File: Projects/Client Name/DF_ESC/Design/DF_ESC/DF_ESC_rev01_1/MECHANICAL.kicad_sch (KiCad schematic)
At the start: 0 parts

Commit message: libraries & schemtics
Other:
- note added: "03407610395"
- note added: "Muhammad Moiz"
- note added: "moizrai765yt@gmail.com"
- company: (none) -> coVenture
- title: (none) -> MECHANICAL
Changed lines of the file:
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@@
 	(generator_version "8.0")
 	(paper "A4")
+	(title_block
+		(title "MECHANICAL")
+		(date "2025-02-03")
+		(rev "rev01_1")
+		(company "coVenture")
+	)
+	(text "Muhammad Moiz\n"
+		(exclude_from_sim no)
+		(at 210.566 168.656 0)
+		(effects
+			(font
+				(size 1.27 1.27)
+			)
+		)
+	)
+	(text "moizrai765yt@gmail.com\n"
+		(exclude_from_sim no)
+		(at 214.63 171.704 0)
+		(effects
+			(font
+				(size 1.27 1.27)
+			)
+		)
+	)
+	(text "03407610395\n"
+		(exclude_from_sim no)
+		(at 209.55 177.8 0)
+		(effects
+			(font
+				(size 1.27 1.27)
+			)
+		)
+	)
 )

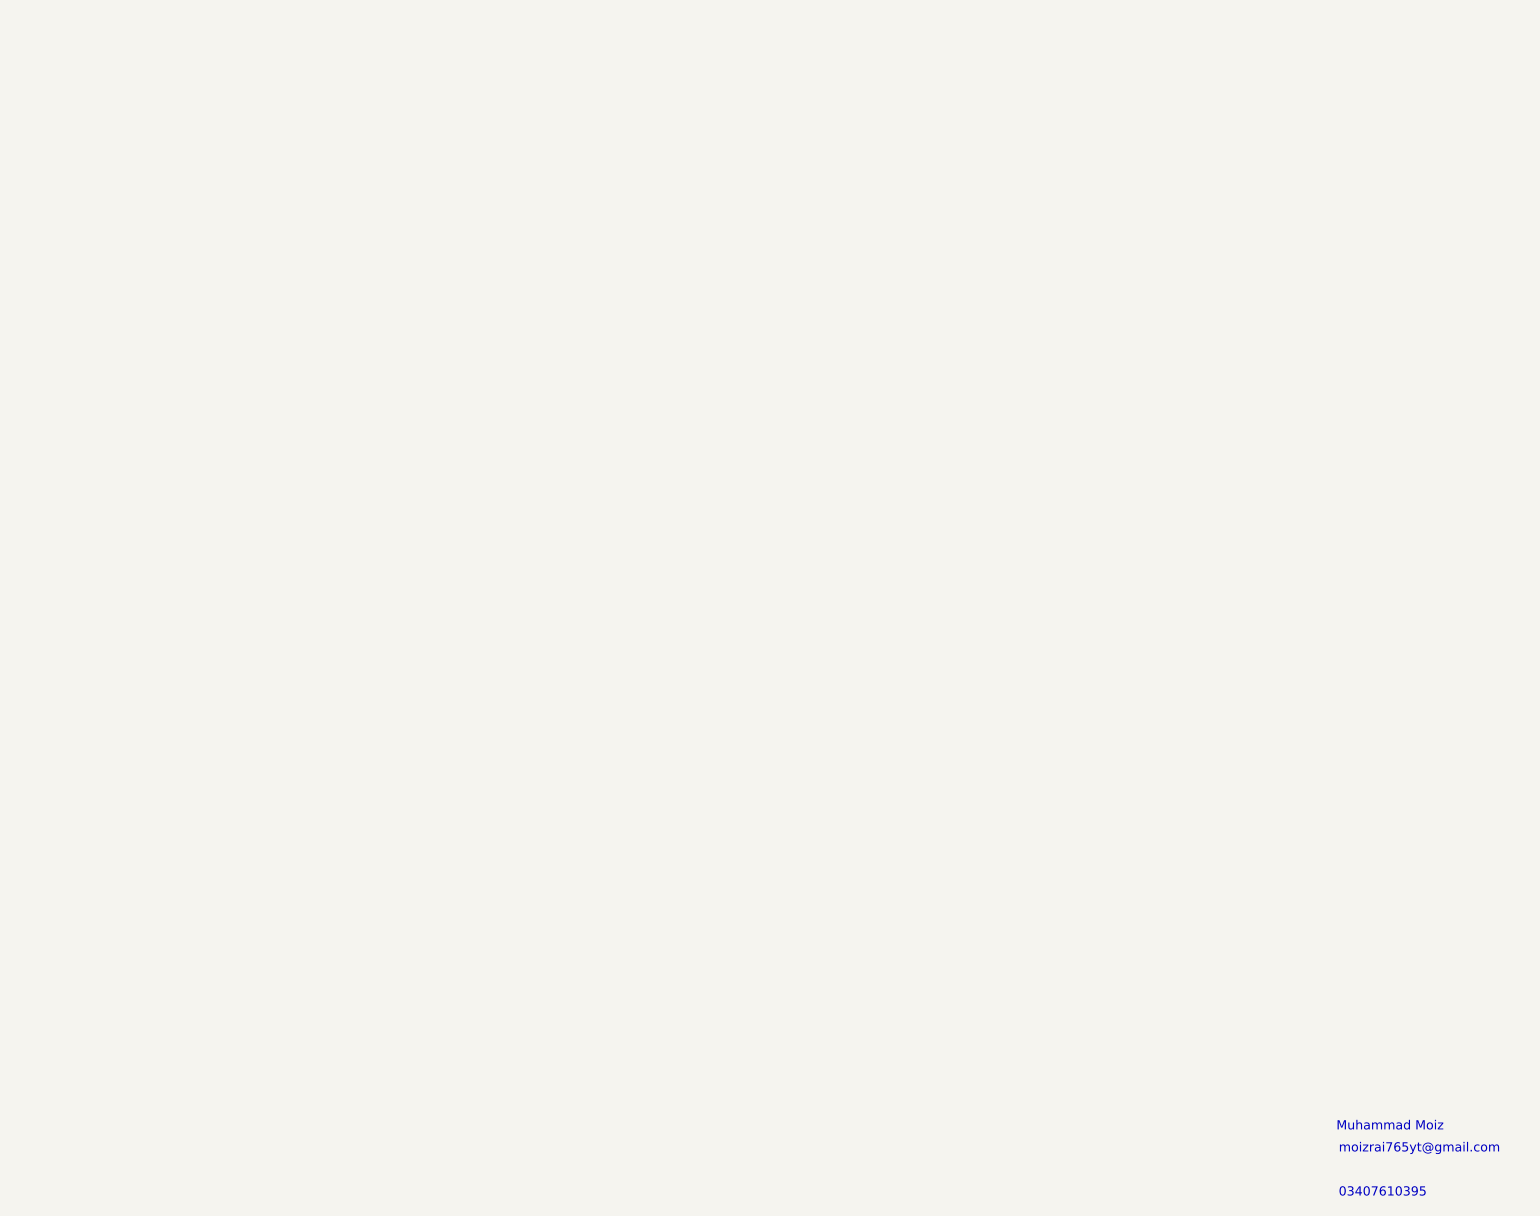
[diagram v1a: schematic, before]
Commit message: updated footprints
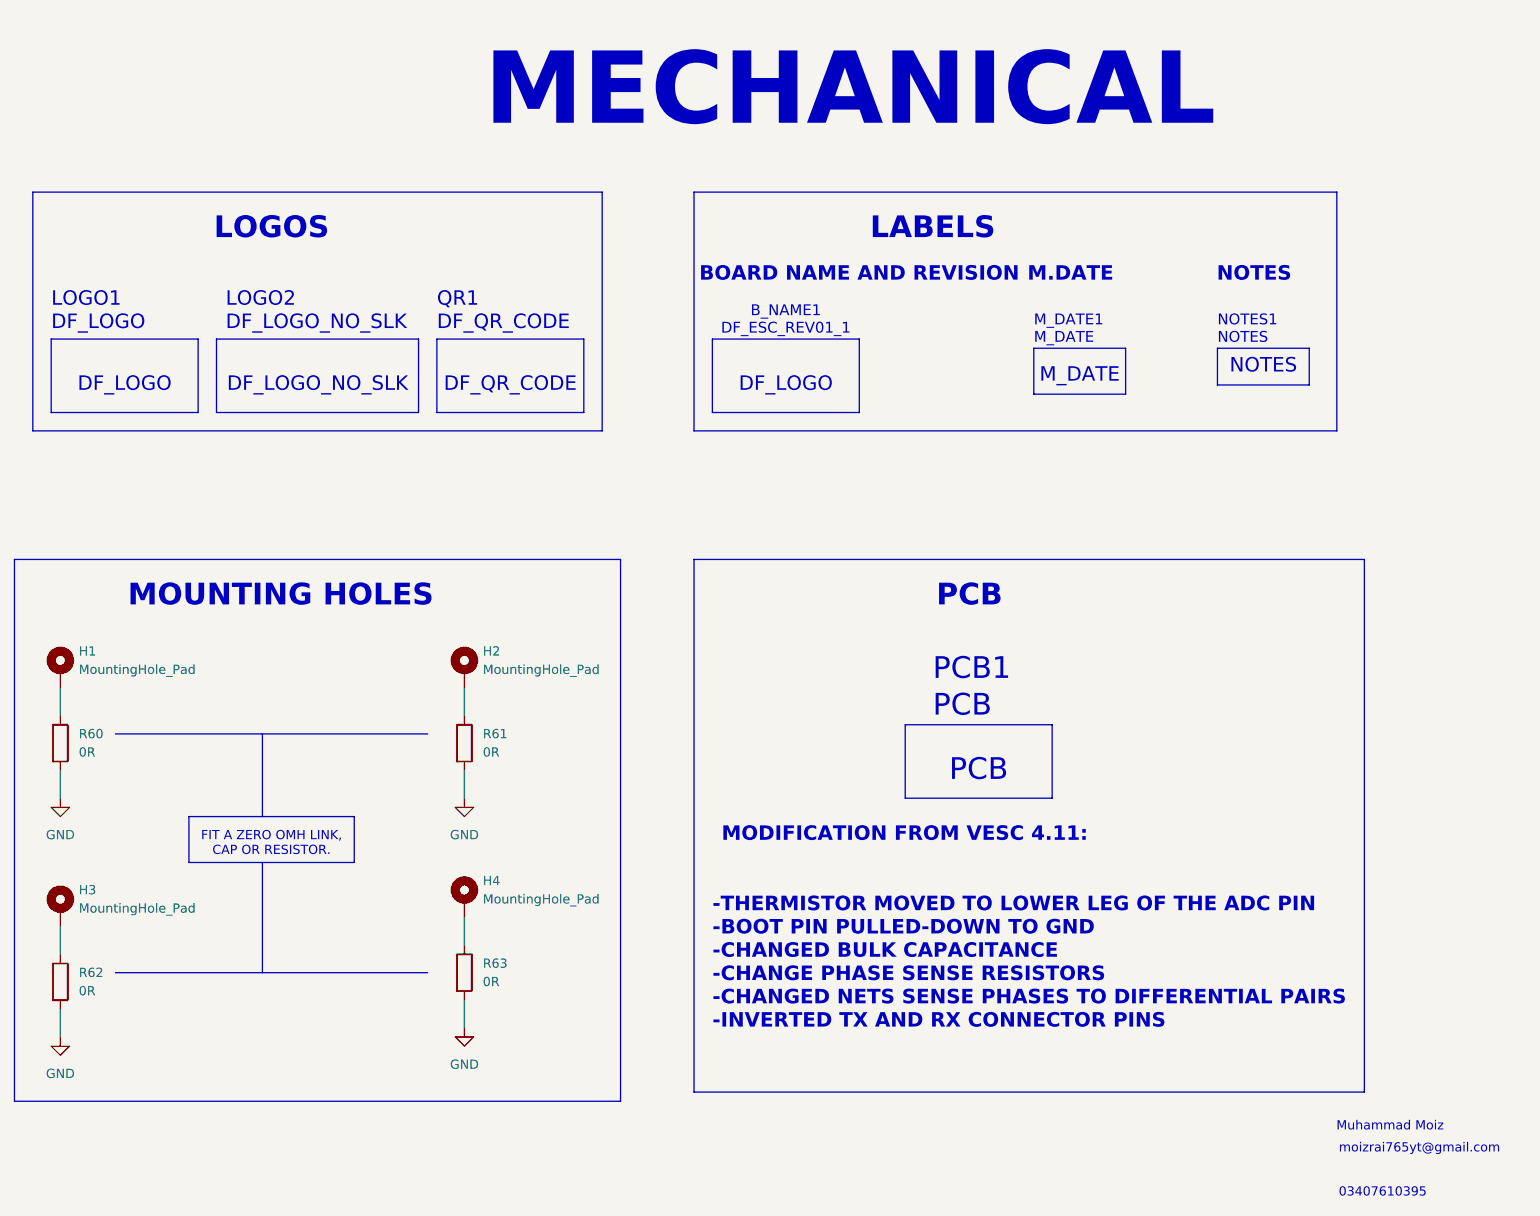
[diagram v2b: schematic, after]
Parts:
- added H1, H2, H3, H4: MountingHole_Pad, MountingHole:MountingHole_2.2mm_M2_DIN965_Pad, symbol Mechanical:MountingHole_Pad
- added R60, R61, R62, R63: 0R, Resistor_SMD:R_0201_0603Metric, symbol Device:R
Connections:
- new net: H1.1, R60.1
- new net: H4.1, R63.1
- new net: H3.1, R62.1
- new net: H2.1, R61.1
- new net GND: R60.2, R61.2, R62.2, R63.2
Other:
- note added: "-THERMISTOR MOVED TO LOWER LEG OF THE ADC PIN -BOOT PIN PULLED-DOWN TO GND -CHANGED BULK CAPACITANCE -CHANGE PHASE SENSE RESISTORS -CHANGED NETS SENSE PHASES TO DIFFERENTIAL PAIRS -INVERTED TX AND RX CONNECTOR PINS"
- note added: "BOARD NAME AND REVISION"
- note added: "B_NAME1 DF_ESC_REV01_1"
- note added: "DF_LOGO"
- note added: "DF_LOGO_NO_SLK"
- note added: "DF_QR_CODE"
- note added: "FIT A ZERO OMH LINK, CAP OR RESISTOR."
- note added: "LABELS"
- note added: "LOGO1 DF_LOGO"
- note added: "LOGO2 DF_LOGO_NO_SLK"
- note added: "LOGOS"
- note added: "M.DATE"
- note added: "MECHANICAL"
- note added: "MODIFICATION FROM VESC 4.11:"
- note added: "MOUNTING HOLES"
- note added: "M_DATE"
- note added: "M_DATE1 M_DATE"
- note added: "NOTES"
- note added: "NOTES1 NOTES"
- note added: "PCB"
- note added: "PCB1"
- note added: "QR1 DF_QR_CODE"
